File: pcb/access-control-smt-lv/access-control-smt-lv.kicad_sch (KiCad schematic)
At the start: 38 parts, among them U1 ESP32-WROOM-E

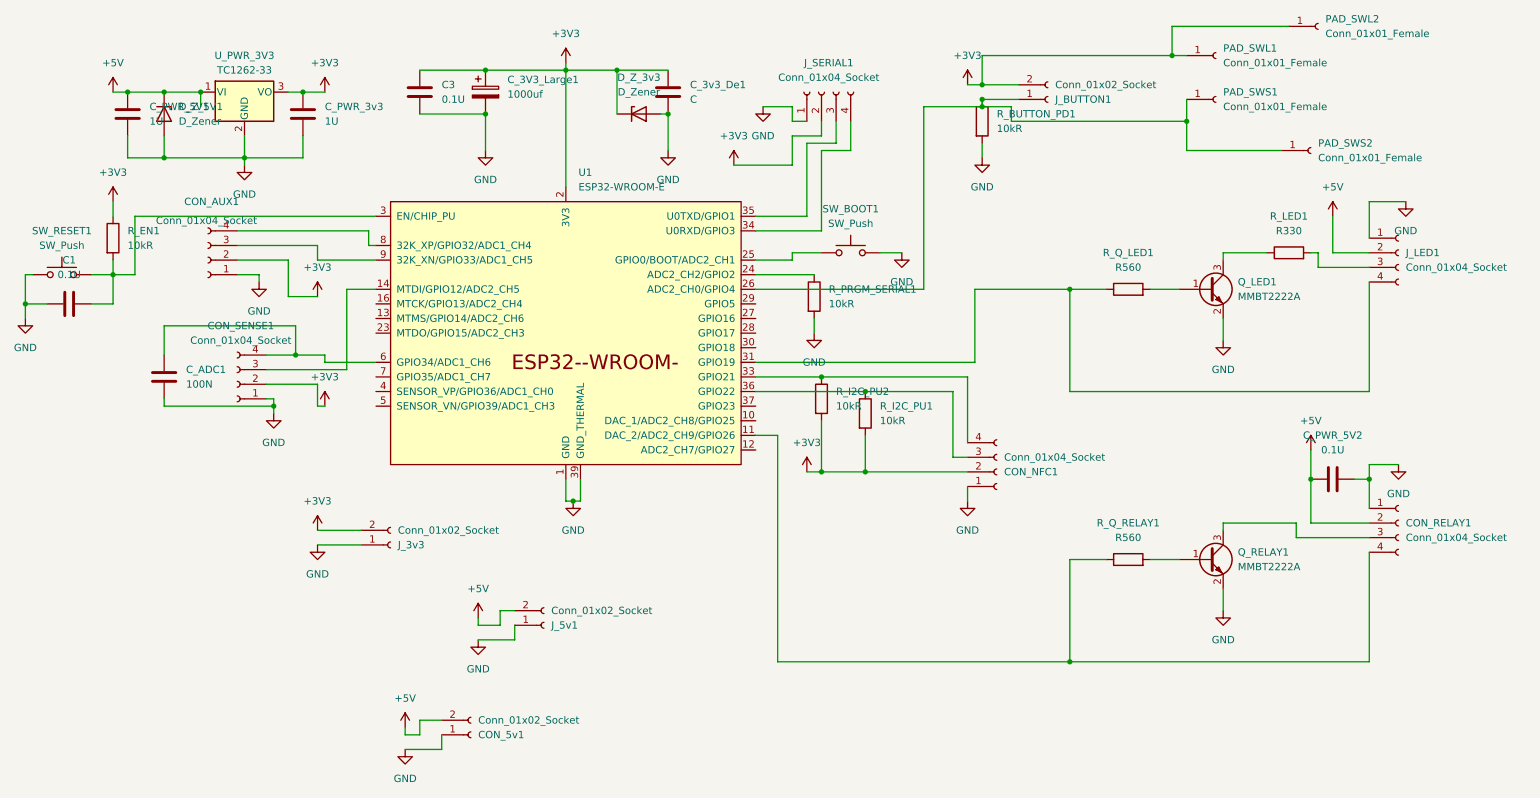
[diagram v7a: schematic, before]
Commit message: Correct compontent value for Tim
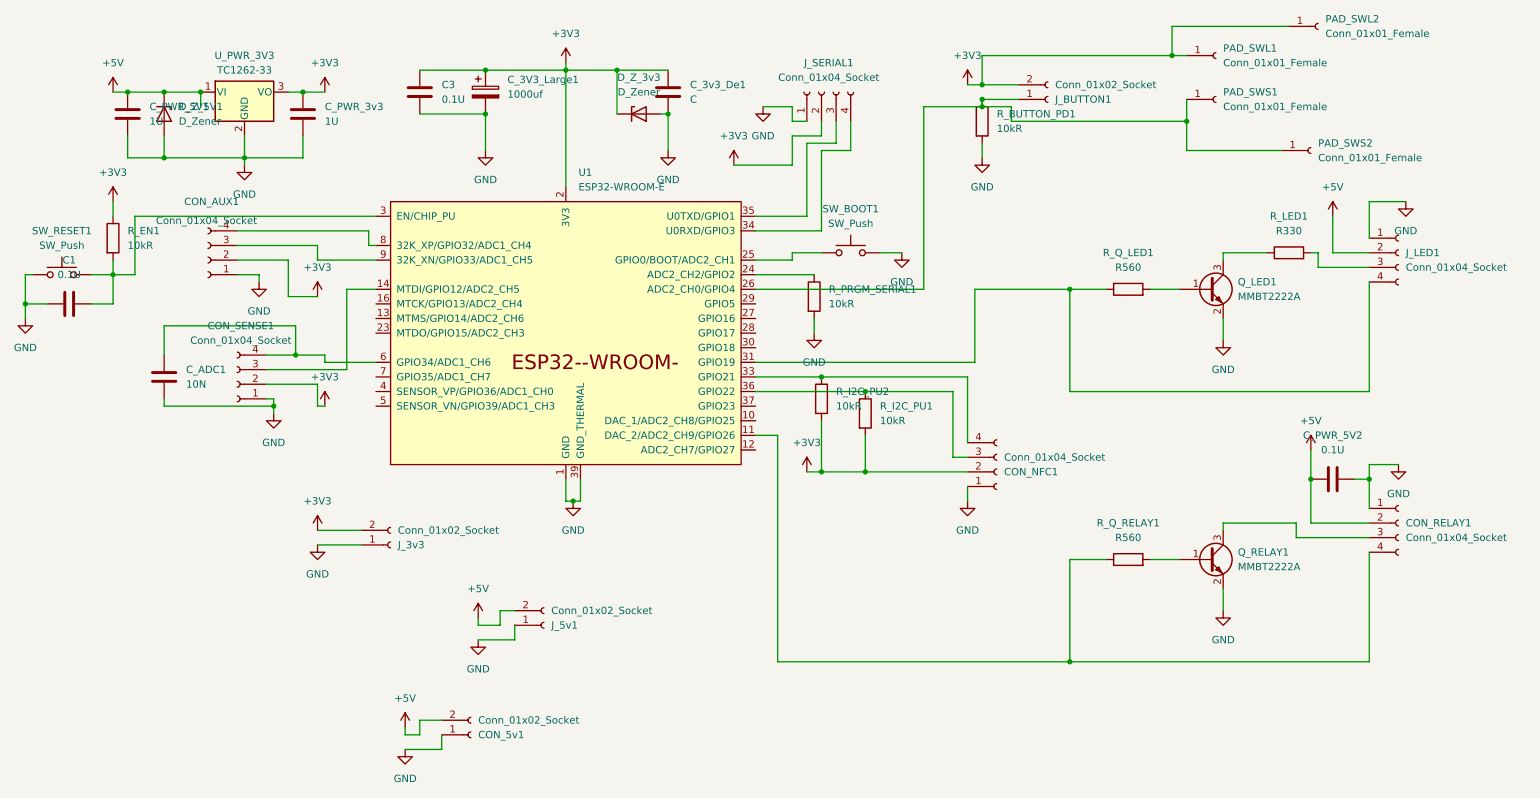
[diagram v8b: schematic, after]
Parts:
- C_ADC1: value 100N -> 10N
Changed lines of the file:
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@@
 (kicad_sch
-	(version 20231120)
+	(version 20250114)
 	(generator "eeschema")
-	(generator_version "8.0")
+	(generator_version "9.0")
 	(paper "A4")
 	(junction
@@
 			)
 		)
-		(property "Value" "100N"
+		(property "Value" "10N"
 			(at 26.67 77.4699 0)
 			(effects
@@
 		)
 	)
+	(embedded_fonts no)
 )
